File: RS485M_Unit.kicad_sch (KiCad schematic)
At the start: 30 parts, among them CN1 CON_GROVE, J1 Conn_01x04, SW1 SW_Push, U1 WB485E, U2 TD1466A, U4 MCU_STC8G1Kxx-8P

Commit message: update readme
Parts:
- removed JP6, JP7: Jumper_2_Open, Jumper:SolderJumper-2_P1.3mm_Open_Pad1.0x1.5mm, symbol Jumper:Jumper_2_Open
- removed SW1: SW_Push, Button_Switch_SMD:SW_Push_SPST_NO_Alps_SKRK, symbol Switch:SW_Push
- added JP6, JP7: Jumper_2_Bridged, Jumper:SolderJumper-2_P1.3mm_Bridged_Pad1.0x1.5mm, symbol Jumper:Jumper_2_Bridged
- D2: footprint Diode_SMD:D_SOD-123F -> Diode_SMD:D_SOD-323F; LCSC C190475 -> (none)
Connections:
- net BUS_A: now also JP6.1 (A)
- net BUS_B: now also JP7.1 (A)
- net at R6.2: now also JP7.2 (B)
- net at R5.2: now also JP6.2 (B)

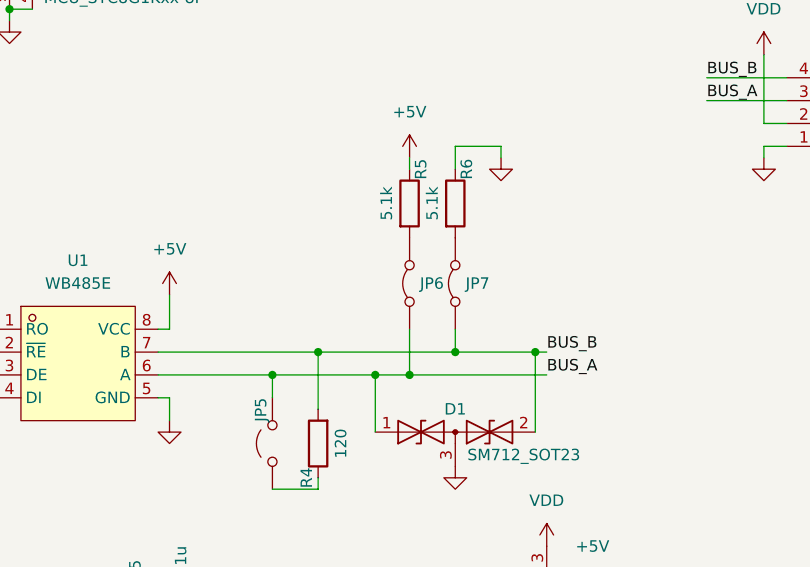
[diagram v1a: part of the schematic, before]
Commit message: add photo, JP6/7 modify
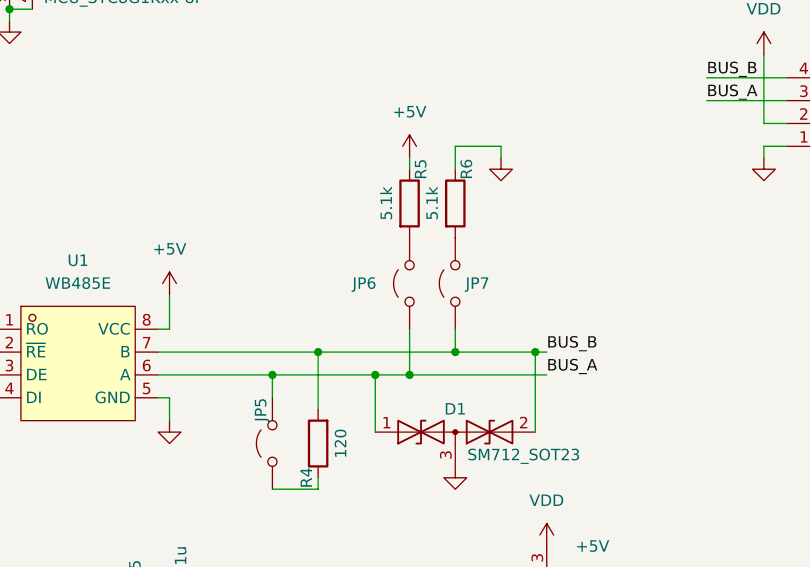
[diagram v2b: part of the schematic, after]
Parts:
- removed JP6, JP7: Jumper_2_Bridged, Jumper:SolderJumper-2_P1.3mm_Bridged_Pad1.0x1.5mm, symbol Jumper:Jumper_2_Bridged
- added JP6, JP7: Jumper_2_Open, Jumper:SolderJumper-2_P1.3mm_Open_Pad1.0x1.5mm, symbol Jumper:Jumper_2_Open
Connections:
- net BUS_A: now also JP6.1 (A)
- net BUS_B: now also JP7.1 (A)
- net at R6.2: now also JP7.2 (B)
- net at R5.2: now also JP6.2 (B)
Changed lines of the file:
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@@
+	)
+	(symbol
+		(lib_id "Jumper:Jumper_2_Open")
+		(at 142.24 110.49 90)
+		(unit 1)
+		(exclude_from_sim no)
+		(in_bom yes)
+		(on_board yes)
+		(dnp no)
+		(fields_autoplaced yes)
+		(property "Reference" "JP7"
+			(at 143.383 110.49 90)
+			(effects
+				(font
+					(size 1.27 1.27)
+				)
+				(justify right)
+			)
+		)
+		(property "Value" "Jumper_2_Open"
+			(at 143.383 111.7021 90)
+			(effects
+				(font
+					(size 1.27 1.27)
+				)
+				(justify right)
+				(hide yes)
+			)
+		)
+		(property "Footprint" "Jumper:SolderJumper-2_P1.3mm_Open_Pad1.0x1.5mm"
+			(at 142.24 110.49 0)
+			(effects
+				(font
+					(size 1.27 1.27)
+				)
+				(hide yes)
+			)
+		)
+		(property "Datasheet" "~"
+			(at 142.24 110.49 0)
+			(effects
+				(font
+					(size 1.27 1.27)
+				)
+				(hide yes)
+			)
+		)
+		(property "Description" "Jumper, 2-pole, open"
+			(at 142.24 110.49 0)
+			(effects
+				(font
+					(size 1.27 1.27)
+				)
+				(hide yes)
+			)
+		)
+		(pin "2"
+		)
+		(pin "1"
+		)
+		(instances
+			(project "RS485M_Unit"
+				(path "/760cbfba-7c24-4b25-8710-3bc574515a2e"
+					(reference "JP7")
+					(unit 1)
+				)
+			)
+		)
 	)
 	(symbol
@@
 	)
 	(symbol
+		(lib_id "Jumper:Jumper_2_Open")
+		(at 137.16 110.49 90)
+		(unit 1)
+		(exclude_from_sim no)
+		(in_bom yes)
+		(on_board yes)
+		(dnp no)
+		(property "Reference" "JP6"
+			(at 130.81 110.49 90)
+			(effects
+				(font
+					(size 1.27 1.27)
+				)
+				(justify right)
+			)
+		)
+		(property "Value" "Jumper_2_Open"
+			(at 138.303 111.7021 90)
+			(effects
+				(font
+					(size 1.27 1.27)
+				)
+				(justify right)
+				(hide yes)
+			)
+		)
+		(property "Footprint" "Jumper:SolderJumper-2_P1.3mm_Open_Pad1.0x1.5mm"
+			(at 137.16 110.49 0)
+			(effects
+				(font
+					(size 1.27 1.27)
+				)
+				(hide yes)
+			)
+		)
+		(property "Datasheet" "~"
+			(at 137.16 110.49 0)
+			(effects
+				(font
+					(size 1.27 1.27)
+				)
+				(hide yes)
+			)
+		)
+		(property "Description" "Jumper, 2-pole, open"
+			(at 137.16 110.49 0)
+			(effects
+				(font
+					(size 1.27 1.27)
+				)
+				(hide yes)
+			)
+		)
+		(pin "2"
+		)
+		(pin "1"
+		)
+		(instances
+			(project ""
+				(path "/760cbfba-7c24-4b25-8710-3bc574515a2e"
+					(reference "JP6")
+					(unit 1)
+				)
+			)
+		)
+	)
+	(symbol
 		(lib_id "Device:R")
 		(at 81.28 107.95 0)
@@
 				(path "/760cbfba-7c24-4b25-8710-3bc574515a2e"
 					(reference "C5")
-					(unit 1)
-				)
-			)
-		)
-	)
-	(symbol
-		(lib_id "Jumper:Jumper_2_Bridged")
-		(at 142.24 110.49 90)
-		(unit 1)
-		(exclude_from_sim no)
-		(in_bom yes)
-		(on_board yes)
-		(dnp no)
-		(fields_autoplaced yes)
-		(property "Reference" "JP7"
-			(at 143.383 110.49 90)
-			(effects
-				(font
-					(size 1.27 1.27)
-				)
-				(justify right)
-			)
-		)
-		(property "Value" "Jumper_2_Bridged"
-			(at 143.383 111.7021 90)
-			(effects
-				(font
-					(size 1.27 1.27)
-				)
-				(justify right)
-				(hide yes)
-			)
-		)
-		(property "Footprint" "Jumper:SolderJumper-2_P1.3mm_Bridged_Pad1.0x1.5mm"
-			(at 142.24 110.49 0)
-			(effects
-				(font
-					(size 1.27 1.27)
-				)
-				(hide yes)
-			)
-		)
-		(property "Datasheet" "~"
-			(at 142.24 110.49 0)
-			(effects
-				(font
-					(size 1.27 1.27)
-				)
-				(hide yes)
-			)
-		)
-		(property "Description" "Jumper, 2-pole, closed/bridged"
-			(at 142.24 110.49 0)
-			(effects
-				(font
-					(size 1.27 1.27)
-				)
-				(hide yes)
-			)
-		)
-		(pin "2"
-		)
-		(pin "1"
-		)
-		(instances
-			(project "RS485M_Unit"
-				(path "/760cbfba-7c24-4b25-8710-3bc574515a2e"
-					(reference "JP7")
 					(unit 1)
 				)
@@
 					(unit 1)
 				)
-			)
-		)
-	)
-	(symbol
-		(lib_id "Jumper:Jumper_2_Bridged")
-		(at 137.16 110.49 90)
-		(unit 1)
-		(exclude_from_sim no)
-		(in_bom yes)
-		(on_board yes)
-		(dnp no)
-		(fields_autoplaced yes)
-		(property "Reference" "JP6"
-			(at 138.303 110.49 90)
-			(effects
-				(font
-					(size 1.27 1.27)
-				)
-				(justify right)
-			)
-		)
-		(property "Value" "Jumper_2_Bridged"
-			(at 138.303 111.7021 90)
-			(effects
-				(font
-					(size 1.27 1.27)
-				)
-				(justify right)
-				(hide yes)
-			)
-		)
-		(property "Footprint" "Jumper:SolderJumper-2_P1.3mm_Bridged_Pad1.0x1.5mm"
-			(at 137.16 110.49 0)
-			(effects
-				(font
-					(size 1.27 1.27)
-				)
-				(hide yes)
-			)
-		)
-		(property "Datasheet" "~"
-			(at 137.16 110.49 0)
-			(effects
-				(font
-					(size 1.27 1.27)
-				)
-				(hide yes)
-			)
-		)
-		(property "Description" "Jumper, 2-pole, closed/bridged"
-			(at 137.16 110.49 0)
-			(effects
-				(font
-					(size 1.27 1.27)
-				)
-				(hide yes)
-			)
-		)
-		(pin "2"
-		)
-		(pin "1"
-		)
-		(instances
-			(project ""
-				(path "/760cbfba-7c24-4b25-8710-3bc574515a2e"
-					(reference "JP6")
-					(unit 1)
-				)
